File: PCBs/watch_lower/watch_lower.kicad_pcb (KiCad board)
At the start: 2 copper layers, 17 parts, among them J1 AXG220144, U1 MAX30102EFD+T, U2 DRV2605LYZFR

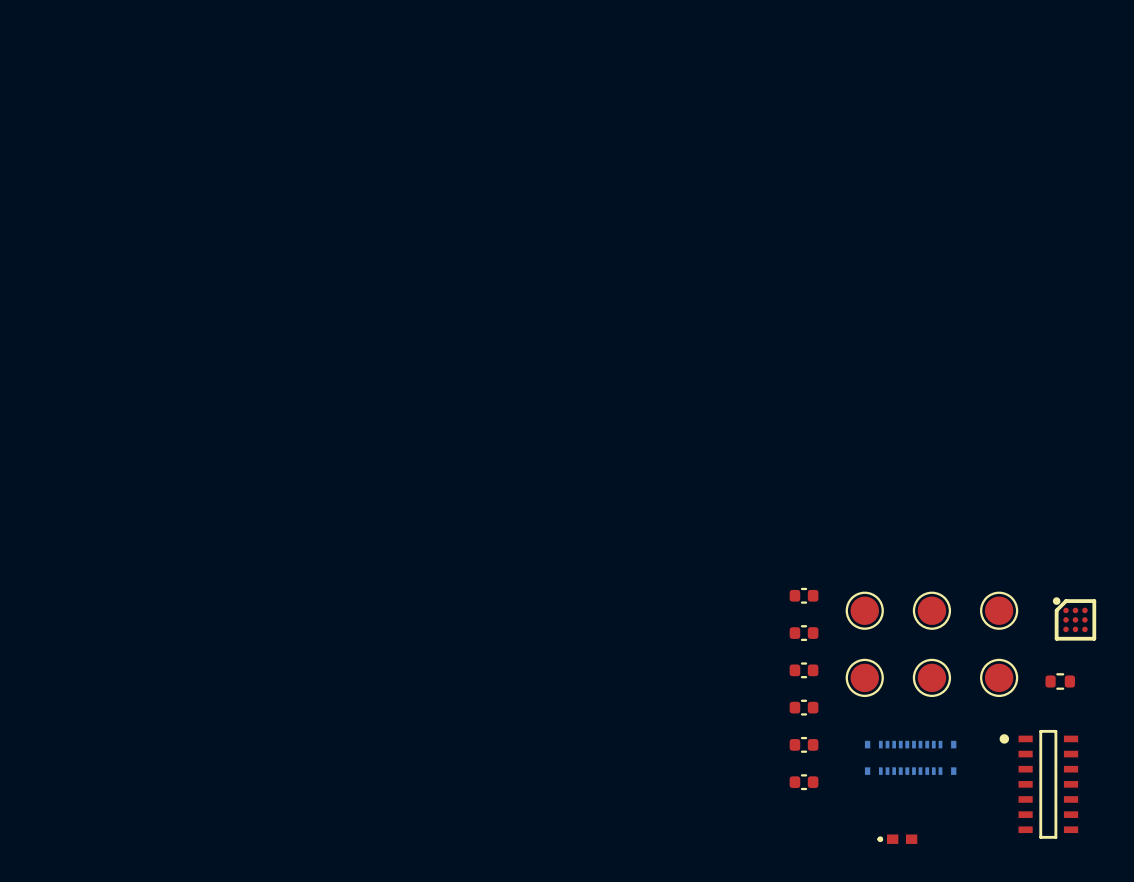
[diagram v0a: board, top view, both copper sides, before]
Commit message: RFID PCB Done, started lower flex PCB
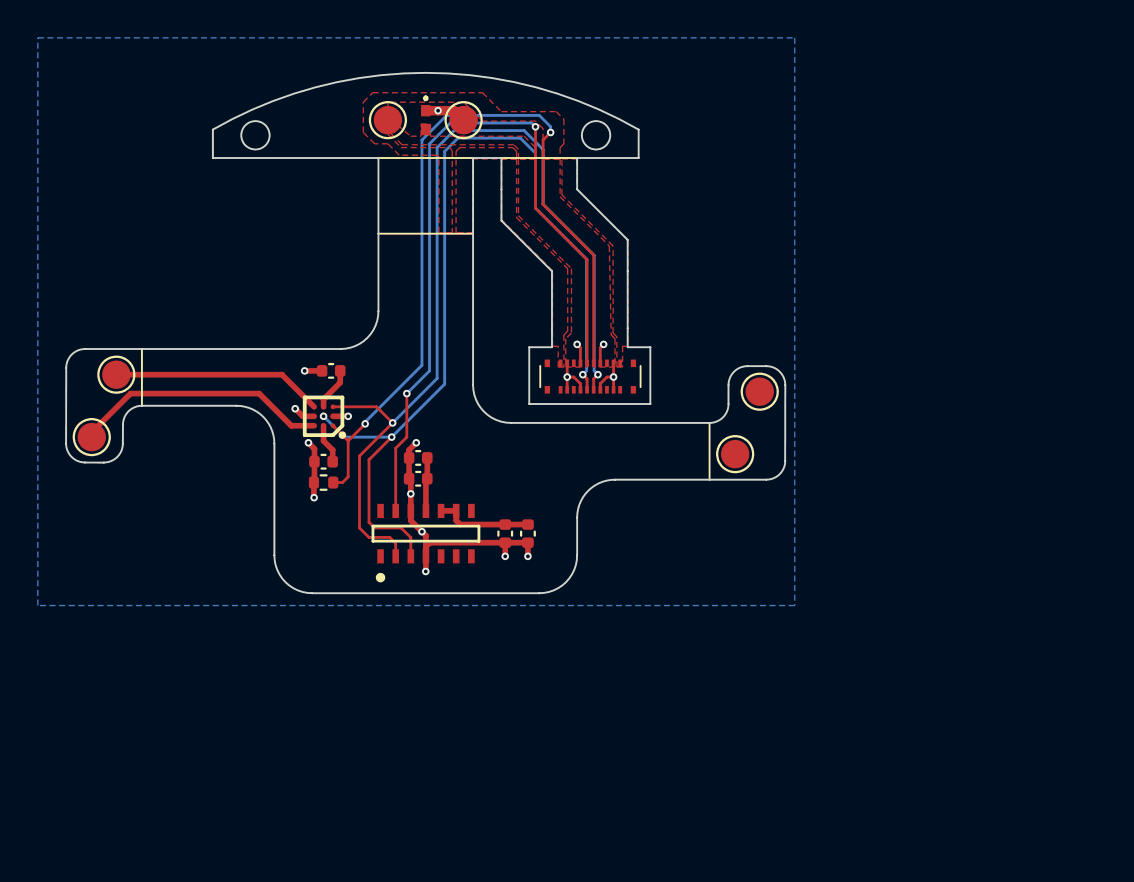
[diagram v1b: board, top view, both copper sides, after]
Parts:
- added U101: Watch_Lower_Outline_V1, watch_footprints:Watch Lower Outline V1, F.Cu at (105.5, 67.3)
- J1: moved to F.Cu
- U1: value MAX30102EFD+T -> Val**
- moved TP6 49.3 mm to (89.2, 67.8)
- moved TP5 48.8 mm to (87.8, 71.1)
- moved D1 45.6 mm to (105.5, 54.4), turned to -90 degrees
- moved U2 41.2 mm to (100.1, 70.0), turned to 180 degrees
- moved R1 40.3 mm to (100.1, 73.5), turned to 180 degrees
- moved TP3 38.7 mm to (103.5, 54.4)
- moved TP4 38.5 mm to (107.5, 54.4)
- moved U1 35.5 mm to (105.5, 76.2), turned to 90 degrees
- moved C6 33.1 mm to (100.5, 67.6), turned to 180 degrees
- moved C5 29.5 mm to (100.1, 72.4), turned to 180 degrees
- moved J1 26.3 mm to (114.2, 67.9), turned to 0 degrees
- moved C4 23.7 mm to (105.1, 73.3), turned to 180 degrees
- moved C3 23.3 mm to (105.1, 72.2), turned to 180 degrees
- moved C2 16.6 mm to (109.7, 76.2), turned to -90 degrees
- moved TP2 16.1 mm to (123.2, 68.7)
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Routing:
- net /SCL: track 0.00 -> 48.6 mm, vias 0 -> 2
- net /SDA: track 0.00 -> 48.1 mm, vias 0 -> 3
- net /LRA_EN: track 0.00 -> 42.8 mm, vias 0 -> 2
- net /HR_INT: track 0.00 -> 39.9 mm, vias 0 -> 2
- net GND: track 0.00 -> 30.2 mm, vias 0 -> 16
- net /M+: track 0.00 -> 13.6 mm
- net /M-: track 0.00 -> 11.2 mm
- net +3V3: track 0.00 -> 5.19 mm
- net +1V8: track 0.00 -> 2.83 mm
- net +VBAT: track 0.00 -> 2.26 mm
- net /REG: track 0.00 -> 2.10 mm
- added copper zone on F.Cu, net +1V8
- added copper zone on F.Cu, net +3V3
- added copper zone on F.Cu, net +VBAT
- added copper zone on B.Cu, net GND
- added copper zone on F.Cu, net VBUS
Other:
- board outline added: 38 x 27.5 mm
- rule pad_to_mask_clearance: 0 -> 0.1

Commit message: Flex PCB finished. Need to rotate RFID transponder coil.
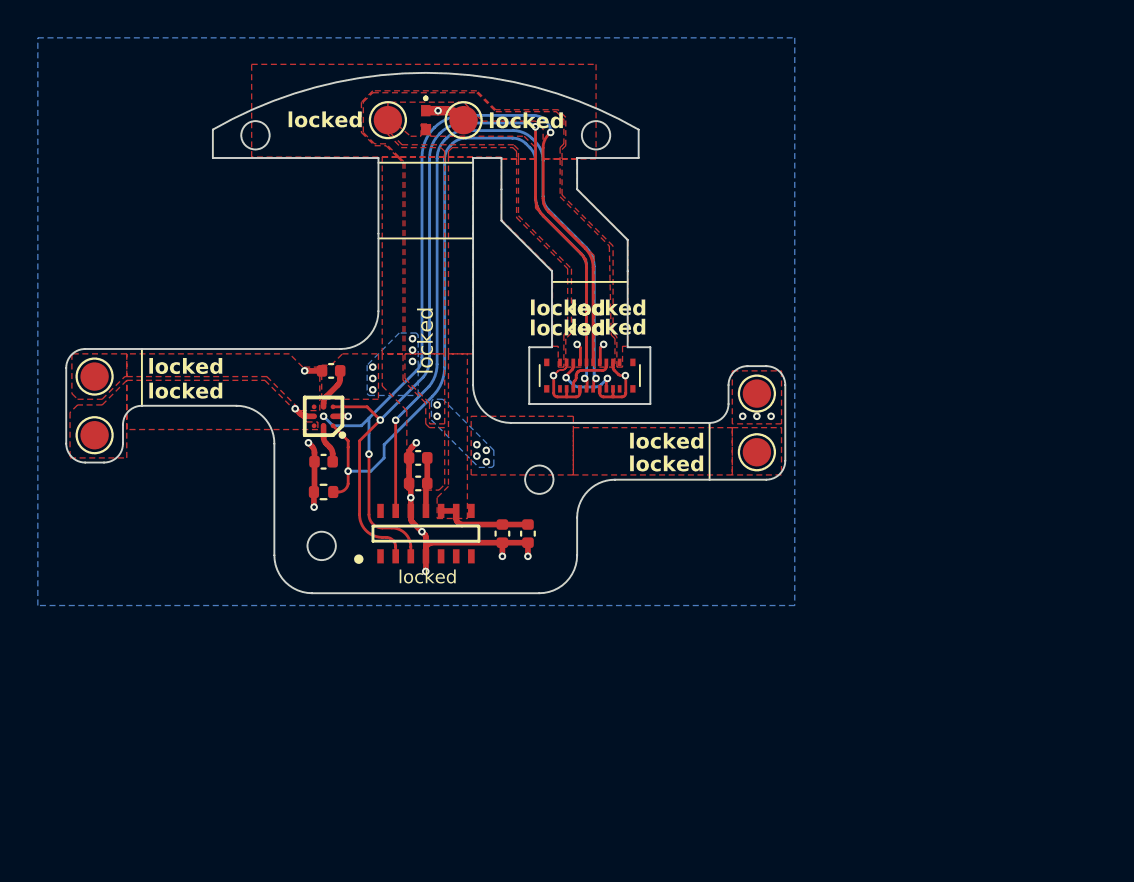
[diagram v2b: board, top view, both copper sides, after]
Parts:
- moved TP6 1.15 mm to (88.0, 67.9)
- moved TP1 1.15 mm to (123.0, 71.9)
- moved R1 0.50 mm to (100.1, 74.0)
- moved C4 0.25 mm to (105.1, 73.5)
- moved TP2 0.18 mm to (123.0, 68.8)
- moved TP5 0.18 mm to (88.0, 71.0)
- moved C2 0.15 mm to (109.5, 76.2)
- moved J1 0.06 mm to (114.2, 67.8)
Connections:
- J1 pad 1: +1V8 -> +3V3
- J1 pad 10: /HR_INT -> /LRA_EN
- J1 pad 11: /SCL -> /SDA
- J1 pad 12: /LRA_EN -> /HR_INT
- J1 pad 15: VBUS -> +VBAT
- J1 pad 16: +VBAT -> VBUS
- J1 pad 19: +3V3 -> +1V8
- J1 pad 2: +3V3 -> unconnected-(J1-Pad2)
- J1 pad 20: +1V8 -> unconnected-(J1-Pad20)
- J1 pad 5: +VBAT -> VBUS
- J1 pad 6: VBUS -> +VBAT
- J1 pad 9: /SDA -> /SCL
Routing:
- net /M+: track 13.6 -> 0.00 mm
- net /M-: track 11.2 -> 0.00 mm
- net VBUS: track 0.00 -> 4.05 mm, vias 0 -> 2
- net GND: track 30.2 -> 34.0 mm, vias 16 -> 19
- net +VBAT: track 2.26 -> 5.04 mm, vias 0 -> 12
- net /SCL: track 48.6 -> 46.6 mm
- added copper zone on B.Cu, net +VBAT
- added copper zone on F.Cu, net /M+
- added copper zone on F.Cu, net /M-
- added copper zone on F.Cu, net GND
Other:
- outline, holes or cut-outs redrawn
- board text added: "locked"

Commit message: 3D Modelling complete, need to rework some PCBs
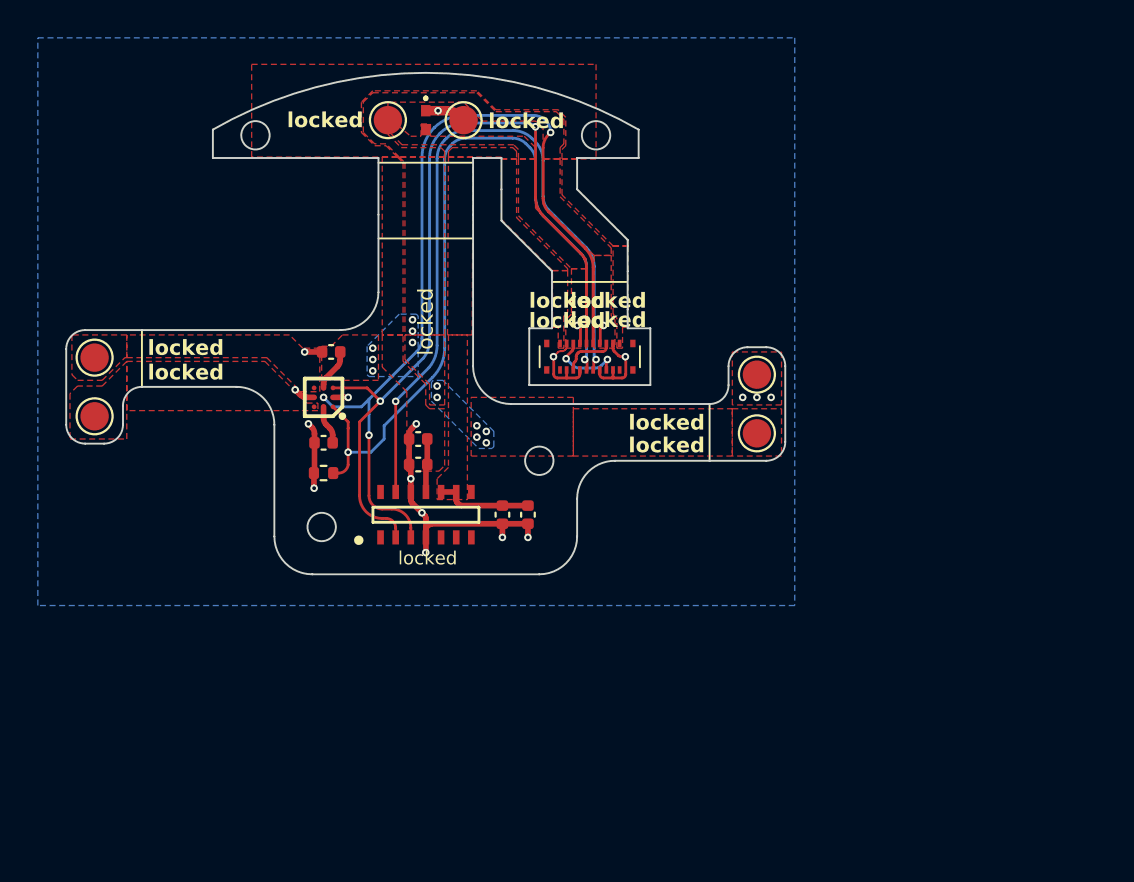
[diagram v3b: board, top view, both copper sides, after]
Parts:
- moved C1 1.00 mm to (110.9, 75.2)
- moved C2 1.00 mm to (109.5, 75.2)
- moved C3 1.00 mm to (105.1, 71.2)
- moved C4 1.00 mm to (105.1, 72.5)
- moved C5 1.00 mm to (100.1, 71.4)
- moved C6 1.00 mm to (100.5, 66.6)
- moved J1 1.00 mm to (114.2, 66.8)
- moved R1 1.00 mm to (100.1, 73.0)
- moved TP1 1.00 mm to (123.0, 70.9)
- moved TP2 1.00 mm to (123.0, 67.8)
- moved TP5 1.00 mm to (88.0, 70.0)
- moved TP6 1.00 mm to (88.0, 66.9)
- moved U1 1.00 mm to (105.5, 75.2)
- moved U2 1.00 mm to (100.1, 69.0)
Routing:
- net /SDA: track 48.1 -> 46.1 mm
- net /LRA_EN: track 42.8 -> 40.8 mm
- net /HR_INT: track 39.9 -> 37.9 mm
- net /SCL: track 46.6 -> 44.6 mm
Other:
- board size 38 x 27.5 mm -> 38 x 26.5 mm

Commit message: RFID Module v1.1 complete (+default firmware)
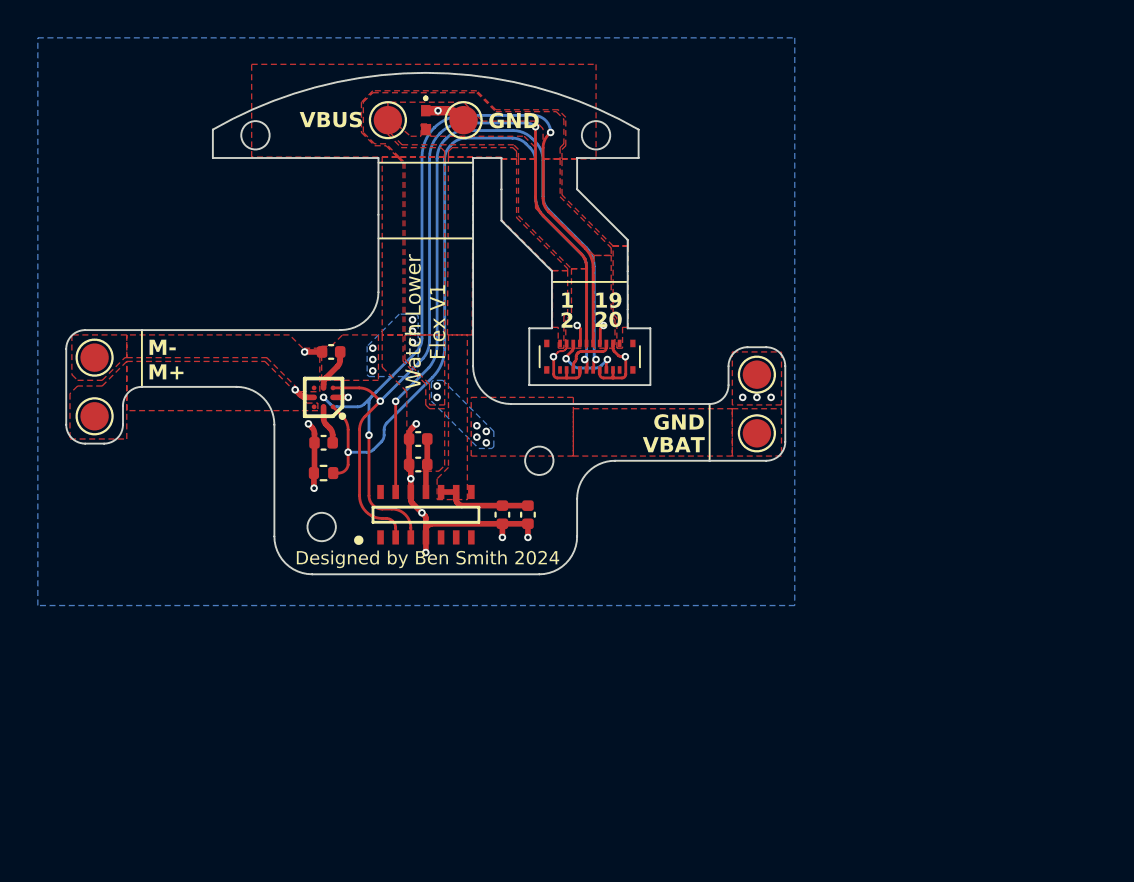
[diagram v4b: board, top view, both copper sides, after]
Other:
- board text added: "1"
- board text added: "19"
- board text added: "2"
- board text added: "20"
- board text added: "Designed by Ben Smith 2024"
- board text added: "GND"
- board text added: "M+"
- board text added: "M-"
- board text added: "Stiffener: Stainless steel Stiffener thickness: 0.2mm Stiffener location: Bottom side"
- board text added: "VBAT"
- board text added: "VBUS"
- board text added: "Watch Lower Flex V1"
- board text removed: "locked"

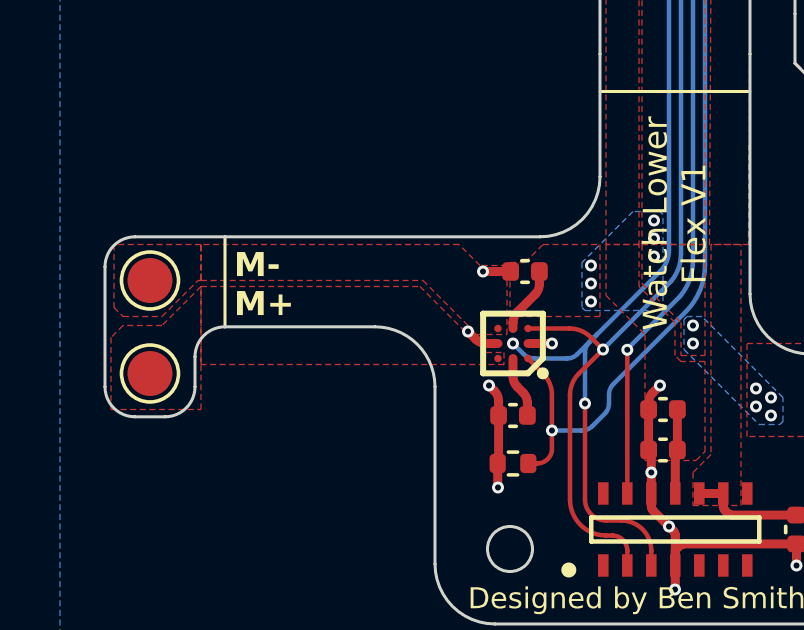
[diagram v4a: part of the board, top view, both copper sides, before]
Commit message: Flex PCB and RFID PCB ordered.
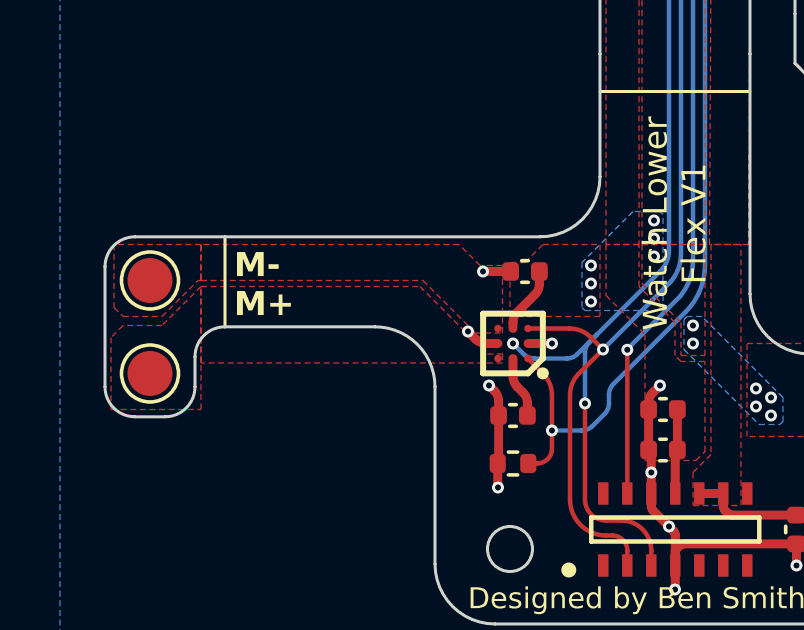
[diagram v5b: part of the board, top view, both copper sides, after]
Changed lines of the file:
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@@
         (xy 89.7 66.9)
         (xy 97.1 66.9)
-        (xy 98.9 68.7)
-        (xy 99.9 68.7)
-        (xy 99.9 66.4)
+        (xy 98.85 68.65)
+        (xy 99.75 68.65)
+        (xy 99.75 66.4)
         (xy 99 66.4)
         (xy 98.3 65.7)
@@
         (xy 116.2 60.7)
         (xy 116.2 61)
+      )
+    )
+  )
+  (zone (net 0) (net_name "") (layer "F.Cu") (hatch edge 0.5)
+    (connect_pads (clearance 0))
+    (min_thickness 0.25) (filled_areas_thickness no)
+    (keepout (tracks allowed) (vias allowed) (pads allowed) (copperpour not_allowed) (footprints allowed))
+    (fill (thermal_gap 0.5) (thermal_bridge_width 0.5))
+    (polygon
+      (pts
+        (xy 100.3 66.1)
+        (xy 100.7 66.1)
+        (xy 100.7 67)
+        (xy 100.3 67)
       )
     )
@@
     )
   )
+  (zone (net 0) (net_name "") (layer "F.Cu") (hatch edge 0.5)
+    (connect_pads (clearance 0))
+    (min_thickness 0.25) (filled_areas_thickness no)
+    (keepout (tracks allowed) (vias allowed) (pads allowed) (copperpour not_allowed) (footprints allowed))
+    (fill (thermal_gap 0.5) (thermal_bridge_width 0.5))
+    (polygon
+      (pts
+        (xy 107.3 73.5)
+        (xy 107.7 73.1)
+        (xy 107.7 74.4)
+        (xy 107.3 74.4)
+      )
+    )
+  )
   (zone (net 2) (net_name "GND") (layer "F.Cu") (hatch edge 0.5)
     (priority 10)
@@
         (xy 86.7 71.2)
         (xy 89.7 71.2)
+      )
+    )
+  )
+  (zone (net 0) (net_name "") (layer "F.Cu") (hatch edge 0.5)
+    (connect_pads (clearance 0))
+    (min_thickness 0.25) (filled_areas_thickness no)
+    (keepout (tracks allowed) (vias allowed) (pads allowed) (copperpour not_allowed) (footprints allowed))
+    (fill (thermal_gap 0.5) (thermal_bridge_width 0.5))
+    (polygon
+      (pts
+        (xy 104.9 70.84)
+        (xy 105.3 70.84)
+        (xy 105.3 72.94)
+        (xy 104.9 72.94)
       )
     )
@@
         (xy 89.7 67.1)
         (xy 97 67.1)
-        (xy 99.2 69.3)
-        (xy 99.8 69.3)
-        (xy 99.8 69.7)
-        (xy 89.7 69.7)
-      )
-    )
+        (xy 99.25 69.35)
+        (xy 99.75 69.35)
+        (xy 99.75 69.65)
+        (xy 89.7 69.65)
+      )
+    )
